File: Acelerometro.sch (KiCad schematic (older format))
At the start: 9 parts, among them Q6 BSS138, Q7 BSS138, U8 MMA7660FC

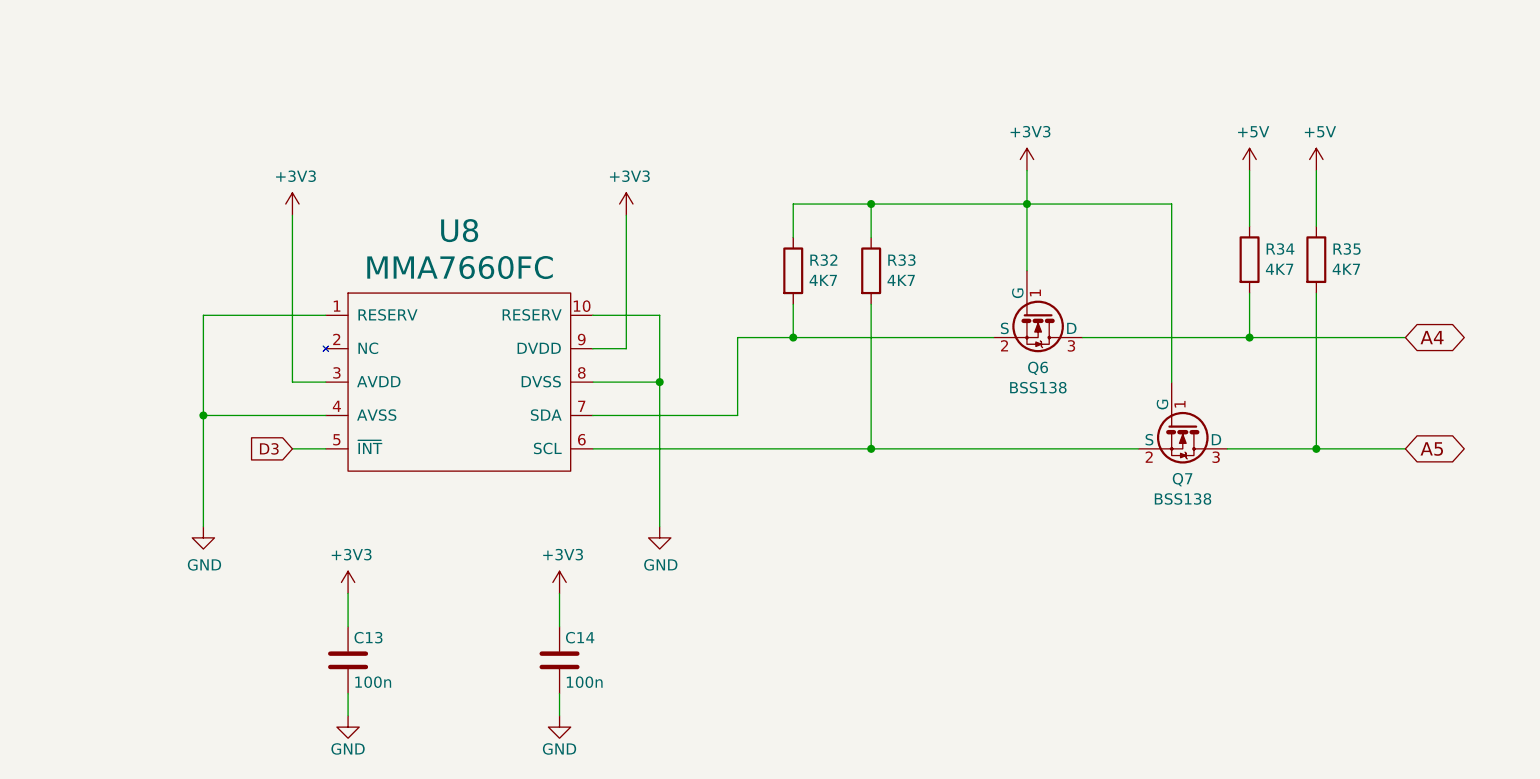
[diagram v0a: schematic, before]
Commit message: Se añade un expansor GPIO al esquema y se elminan registros y codificador
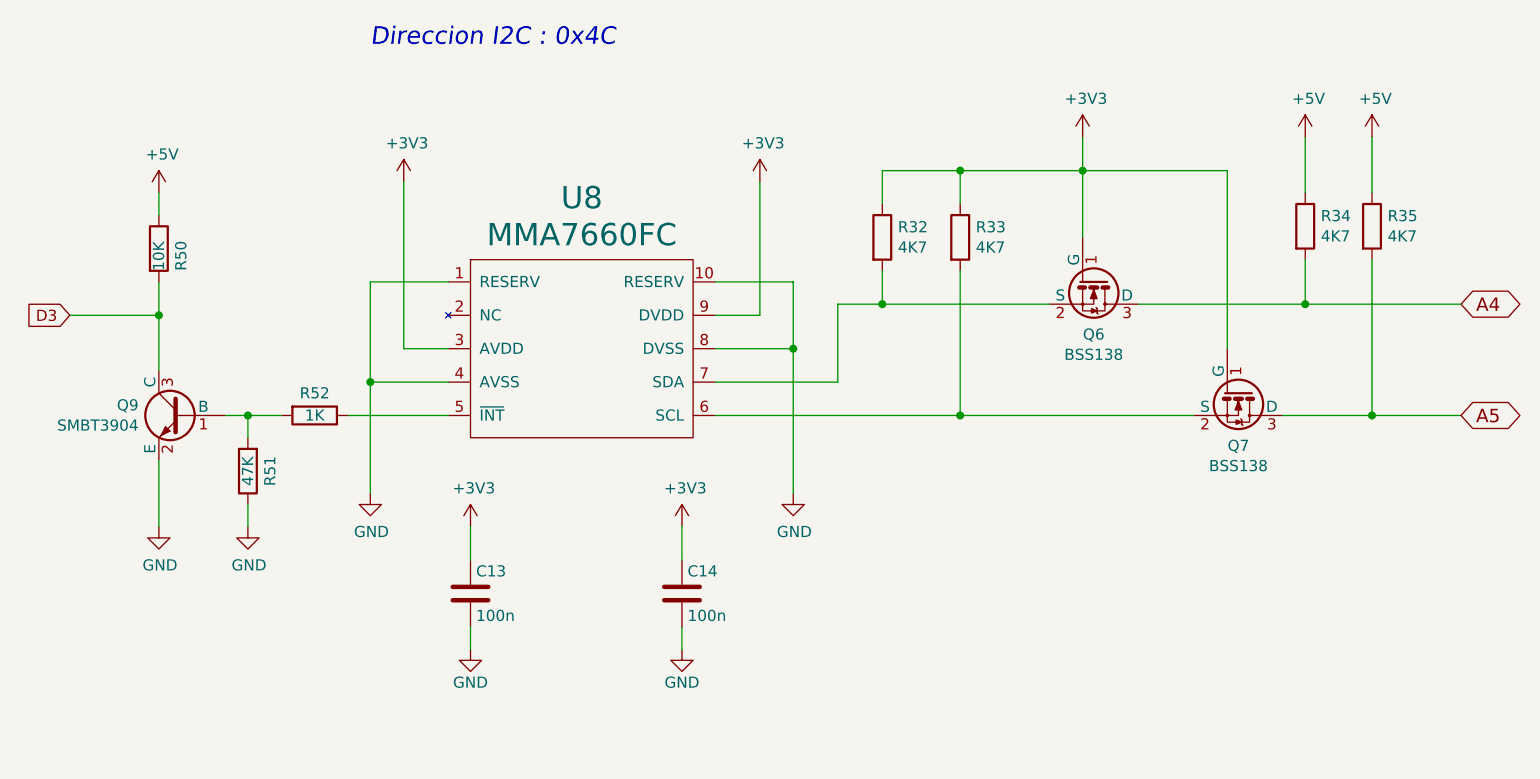
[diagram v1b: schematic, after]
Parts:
- added Q9: SMBT3904, TO_SOT_Packages_SMD:SOT-23, symbol BC849
- added R50: 10K, Resistencias:R_0805, symbol R
- added R51: 47K, Resistencias:R_0805, symbol R
- added R52: 1K, Resistencias:R_0805, symbol R
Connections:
- net +5V: now also R50.1
- net D3: now also Q9.3 (C), R50.2; no longer U8.5 (~INT)
- net GND: now also Q9.2 (E), R51.1
- new net: R52.1, U8.5 (~INT)
- new net: Q9.1 (B), R51.2, R52.2
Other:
- note added: "Direccion I2C : 0x4C"
- moved on the sheet: C13, C14, Q6, Q7, R32, R33, R34, R35, U8

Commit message: finalizada la ubicacion de componentes para la V0.4
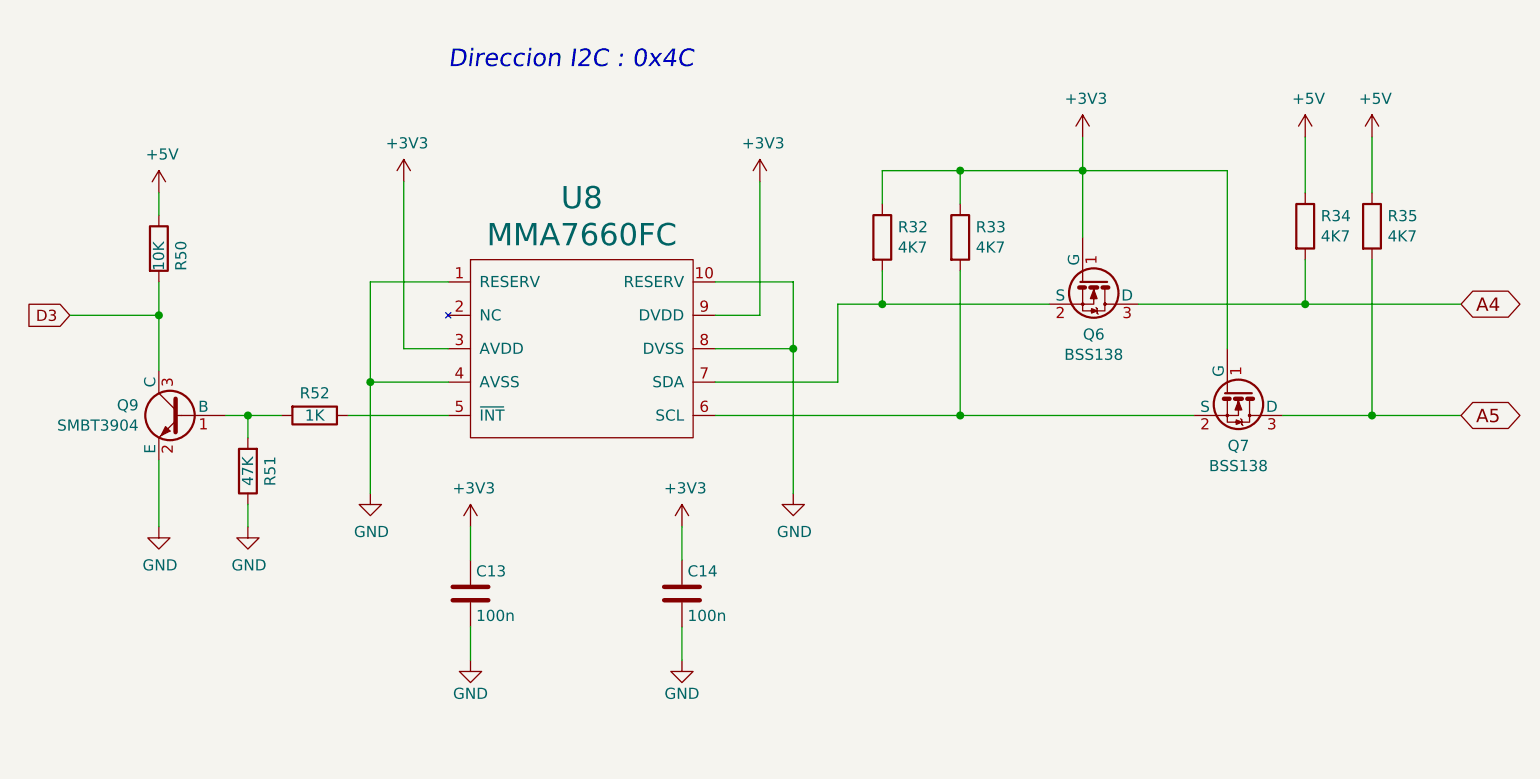
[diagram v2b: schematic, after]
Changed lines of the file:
@@
 	5450 1300 5450 1750
 $Comp
-L +3V3 #PWR064
+L +3V3 #PWR065
 U 1 1 57952AC0
 P 5450 1300
-F 0 "#PWR064" H 5450 1150 50  0001 C CNN
+F 0 "#PWR065" H 5450 1150 50  0001 C CNN
 F 1 "+3V3" H 5465 1473 50  0000 C CNN
 F 2 "" H 5450 1300 50  0000 C CNN
@@
 	6450 1550 6450 1300
 $Comp
-L +5V #PWR065
+L +5V #PWR066
 U 1 1 57952EB0
 P 6450 1300
-F 0 "#PWR065" H 6450 1150 50  0001 C CNN
+F 0 "#PWR066" H 6450 1150 50  0001 C CNN
 F 1 "+5V" H 6465 1473 50  0000 C CNN
 F 2 "" H 6450 1300 50  0000 C CNN
@@
 	6750 1550 6750 1300
 $Comp
-L +5V #PWR066
+L +5V #PWR067
 U 1 1 57952EEB
 P 6750 1300
-F 0 "#PWR066" H 6750 1150 50  0001 C CNN
+F 0 "#PWR067" H 6750 1150 50  0001 C CNN
 F 1 "+5V" H 6765 1473 50  0000 C CNN
 F 2 "" H 6750 1300 50  0000 C CNN
@@
 	4150 1950 4150 2900
 $Comp
-L GND #PWR067
+L GND #PWR068
 U 1 1 579532CA
 P 4150 2900
-F 0 "#PWR067" H 4150 2650 50  0001 C CNN
+F 0 "#PWR068" H 4150 2650 50  0001 C CNN
 F 1 "GND" H 4155 2727 50  0000 C CNN
 F 2 "" H 4150 2900 50  0000 C CNN
@@
 	2250 1950 2250 2900
 $Comp
-L GND #PWR068
+L GND #PWR069
 U 1 1 5795333D
 P 2250 2900
-F 0 "#PWR068" H 2250 2650 50  0001 C CNN
+F 0 "#PWR069" H 2250 2650 50  0001 C CNN
 F 1 "GND" H 2255 2727 50  0000 C CNN
 F 2 "" H 2250 2900 50  0000 C CNN
@@
 	2400 2250 2400 1500
 $Comp
-L +3V3 #PWR069
+L +3V3 #PWR070
 U 1 1 579533C4
 P 2400 1500
-F 0 "#PWR069" H 2400 1350 50  0001 C CNN
+F 0 "#PWR070" H 2400 1350 50  0001 C CNN
 F 1 "+3V3" H 2415 1673 50  0000 C CNN
 F 2 "" H 2400 1500 50  0000 C CNN
@@
 	4000 2100 4000 1500
 $Comp
-L +3V3 #PWR070
+L +3V3 #PWR071
 U 1 1 57953474
 P 4000 1500
-F 0 "#PWR070" H 4000 1350 50  0001 C CNN
+F 0 "#PWR071" H 4000 1350 50  0001 C CNN
 F 1 "+3V3" H 4015 1673 50  0000 C CNN
 F 2 "" H 4000 1500 50  0000 C CNN
@@
 $EndComp
 $Comp
-L GND #PWR071
+L GND #PWR072
 U 1 1 57953EB4
-P 2700 3600
-F 0 "#PWR071" H 2700 3350 50  0001 C CNN
-F 1 "GND" H 2700 3450 50  0000 C CNN
-F 2 "" H 2700 3600 50  0000 C CNN
-F 3 "" H 2700 3600 50  0000 C CNN
-	1    2700 3600
+P 2700 3650
+F 0 "#PWR072" H 2700 3400 50  0001 C CNN
+F 1 "GND" H 2700 3500 50  0000 C CNN
+F 2 "" H 2700 3650 50  0000 C CNN
+F 3 "" H 2700 3650 50  0000 C CNN
+	1    2700 3650
 	1    0    0    -1
 $EndComp
@@
 	2700 3200 2700 3050
 Wire Wire Line
-	2700 3600 2700 3500
+	2700 3650 2700 3500
 $Comp
 L C C14
@@
 $EndComp
 $Comp
-L GND #PWR072
+L GND #PWR073
 U 1 1 57953F7E
-P 3650 3600
-F 0 "#PWR072" H 3650 3350 50  0001 C CNN
-F 1 "GND" H 3650 3450 50  0000 C CNN
-F 2 "" H 3650 3600 50  0000 C CNN
-F 3 "" H 3650 3600 50  0000 C CNN
-	1    3650 3600
+P 3650 3650
+F 0 "#PWR073" H 3650 3400 50  0001 C CNN
+F 1 "GND" H 3650 3500 50  0000 C CNN
+F 2 "" H 3650 3650 50  0000 C CNN
+F 3 "" H 3650 3650 50  0000 C CNN
+	1    3650 3650
 	1    0    0    -1
 $EndComp
@@
 	3650 3200 3650 3050
 Wire Wire Line
-	3650 3600 3650 3500
-$Comp
-L +3V3 #PWR073
+	3650 3650 3650 3500
+$Comp
+L +3V3 #PWR074
 U 1 1 57953FC4
 P 2700 3050
-F 0 "#PWR073" H 2700 2900 50  0001 C CNN
+F 0 "#PWR074" H 2700 2900 50  0001 C CNN
 F 1 "+3V3" H 2715 3223 50  0000 C CNN
 F 2 "" H 2700 3050 50  0000 C CNN
@@
 $EndComp
 $Comp
-L +3V3 #PWR074
+L +3V3 #PWR075
 U 1 1 57954005
 P 3650 3050
-F 0 "#PWR074" H 3650 2900 50  0001 C CNN
+F 0 "#PWR075" H 3650 2900 50  0001 C CNN
 F 1 "+3V3" H 3665 3223 50  0000 C CNN
 F 2 "" H 3650 3050 50  0000 C CNN
@@
 Text GLabel 900  2100 0    50   Input ~ 0
 D3
-Text Notes 2250 900  0    79   Italic 0
+Text Notes 2600 1000 0    79   Italic 0
 Direccion I2C : 0x4C
 $Comp
@@
 	1300 2750 1300 3050
 $Comp
-L GND #PWR075
+L GND #PWR076
 U 1 1 5881543D
 P 1300 3050
-F 0 "#PWR075" H 1300 2800 50  0001 C CNN
+F 0 "#PWR076" H 1300 2800 50  0001 C CNN
 F 1 "GND" H 1305 2877 50  0000 C CNN
 F 2 "" H 1300 3050 50  0000 C CNN
@@
 Connection ~ 1700 2550
 $Comp
-L GND #PWR076
+L GND #PWR077
 U 1 1 58815452
 P 1700 3050
-F 0 "#PWR076" H 1700 2800 50  0001 C CNN
+F 0 "#PWR077" H 1700 2800 50  0001 C CNN
 F 1 "GND" H 1705 2877 50  0000 C CNN
 F 2 "" H 1700 3050 50  0000 C CNN
@@
 	1300 1650 1300 1550
 $Comp
-L +5V #PWR077
+L +5V #PWR078
 U 1 1 58815BF6
 P 1300 1550
-F 0 "#PWR077" H 1300 1400 50  0001 C CNN
+F 0 "#PWR078" H 1300 1400 50  0001 C CNN
 F 1 "+5V" H 1315 1723 50  0000 C CNN
 F 2 "" H 1300 1550 50  0000 C CNN

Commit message: Revisado V0.4. Actualizados gerber y esquemas
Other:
- note added: "Configurar ~INT\nactiva a nivel alto y push-pull"
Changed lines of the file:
@@
 Sheet 13 17
 Title "Acelerometro 3 ejes"
-Date "2017-01-19"
+Date "2017-01-25"
 Rev "V.0.4"
 Comp "NanoPlayBoard"
@@
 $EndComp
 Wire Wire Line
+	1300 1950 1300 2350
+Wire Wire Line
+	2600 2550 2150 2550
+Wire Wire Line
+	1300 2100 900  2100
+$Comp
+L R R50
+U 1 1 58815BED
+P 1300 1800
+F 0 "R50" V 1400 1700 50  0000 L CNN
+F 1 "10K" V 1300 1700 50  0000 L CNN
+F 2 "Resistencias:R_0805" V 1230 1800 50  0001 C CNN
+F 3 "" H 1300 1800 50  0000 C CNN
+F 4 "VISHAY" H 1300 1800 60  0001 C CNN "Fabricante"
+F 5 "CRCW080510K0FKEA" H 1300 1800 60  0001 C CNN "Ref"
+F 6 "1/8W" H 1300 1800 60  0001 C CNN "Potencia"
+F 7 "1%" H 1300 1800 60  0001 C CNN "Tolerancia"
+F 8 "TME" H 1300 1800 60  0001 C CNN "Provedor"
+F 9 "CRCW080510K0FKEA" H 1300 1800 60  0001 C CNN "Ref_Proveedor"
+	1    1300 1800
+	1    0    0    -1
+$EndComp
+Wire Wire Line
+	1300 1650 1300 1550
+$Comp
+L +5V #PWR078
+U 1 1 58815BF6
+P 1300 1550
+F 0 "#PWR078" H 1300 1400 50  0001 C CNN
+F 1 "+5V" H 1315 1723 50  0000 C CNN
+F 2 "" H 1300 1550 50  0000 C CNN
+F 3 "" H 1300 1550 50  0000 C CNN
+	1    1300 1550
+	1    0    0    -1
+$EndComp
+Connection ~ 1300 2100
+Wire Wire Line
 	1600 2550 1850 2550
-Wire Wire Line
-	1300 1950 1300 2350
 Wire Wire Line
 	1300 2750 1300 3050
@@
 	1    0    0    -1
 $EndComp
+$Comp
+L GND #PWR077
+U 1 1 58815452
+P 1700 3050
+F 0 "#PWR077" H 1700 2800 50  0001 C CNN
+F 1 "GND" H 1705 2877 50  0000 C CNN
+F 2 "" H 1700 3050 50  0000 C CNN
+F 3 "" H 1700 3050 50  0000 C CNN
+	1    1700 3050
+	1    0    0    -1
+$EndComp
+Connection ~ 1700 2550
+Wire Wire Line
+	1700 2650 1700 2550
+Wire Wire Line
+	1700 3050 1700 2950
 $Comp
 L R R51
@@
 	-1   0    0    1
 $EndComp
-Wire Wire Line
-	1700 2650 1700 2550
-Connection ~ 1700 2550
-$Comp
-L GND #PWR077
-U 1 1 58815452
-P 1700 3050
-F 0 "#PWR077" H 1700 2800 50  0001 C CNN
-F 1 "GND" H 1705 2877 50  0000 C CNN
-F 2 "" H 1700 3050 50  0000 C CNN
-F 3 "" H 1700 3050 50  0000 C CNN
-	1    1700 3050
-	1    0    0    -1
-$EndComp
-Wire Wire Line
-	1700 3050 1700 2950
-Wire Wire Line
-	2600 2550 2150 2550
-Wire Wire Line
-	1300 2100 900  2100
-$Comp
-L R R50
-U 1 1 58815BED
-P 1300 1800
-F 0 "R50" V 1400 1700 50  0000 L CNN
-F 1 "10K" V 1300 1700 50  0000 L CNN
-F 2 "Resistencias:R_0805" V 1230 1800 50  0001 C CNN
-F 3 "" H 1300 1800 50  0000 C CNN
-F 4 "VISHAY" H 1300 1800 60  0001 C CNN "Fabricante"
-F 5 "CRCW080510K0FKEA" H 1300 1800 60  0001 C CNN "Ref"
-F 6 "1/8W" H 1300 1800 60  0001 C CNN "Potencia"
-F 7 "1%" H 1300 1800 60  0001 C CNN "Tolerancia"
-F 8 "TME" H 1300 1800 60  0001 C CNN "Provedor"
-F 9 "CRCW080510K0FKEA" H 1300 1800 60  0001 C CNN "Ref_Proveedor"
-	1    1300 1800
-	1    0    0    -1
-$EndComp
-Wire Wire Line
-	1300 1650 1300 1550
-$Comp
-L +5V #PWR078
-U 1 1 58815BF6
-P 1300 1550
-F 0 "#PWR078" H 1300 1400 50  0001 C CNN
-F 1 "+5V" H 1315 1723 50  0000 C CNN
-F 2 "" H 1300 1550 50  0000 C CNN
-F 3 "" H 1300 1550 50  0000 C CNN
-	1    1300 1550
-	1    0    0    -1
-$EndComp
-Connection ~ 1300 2100
+Text Notes 1200 3600 0    47   ~ 0
+Configurar ~INT\nactiva a nivel alto y push-pull
 $EndSCHEMATC

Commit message: finalizada V0.4.1 corrige #17, #18 y #19
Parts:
- Q6, Q7: symbol BSS138 -> BSS138-RESCUE-Nano_PB
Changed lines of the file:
@@
 LIBS:Pasivos
 LIBS:Reles
+LIBS:Arduino
 LIBS:Nano_PB-cache
 EELAYER 26 0
@@
 $EndDescr
 $Comp
-L BSS138 Q6
+L BSS138-RESCUE-Nano_PB Q6
 U 1 1 57952913
 P 5500 1950
@@
 	5450 1300 5450 1750
 $Comp
-L +3V3 #PWR057
+L +3V3 #PWR058
 U 1 1 57952AC0
 P 5450 1300
-F 0 "#PWR057" H 5450 1150 50  0001 C CNN
+F 0 "#PWR058" H 5450 1150 50  0001 C CNN
 F 1 "+3V3" H 5465 1473 50  0000 C CNN
 F 2 "" H 5450 1300 50  0000 C CNN
@@
 A5
 $Comp
-L BSS138 Q7
+L BSS138-RESCUE-Nano_PB Q7
 U 1 1 57952D65
 P 6150 2450
@@
 	6450 1550 6450 1300
 $Comp
-L +5V #PWR058
+L +5V #PWR059
 U 1 1 57952EB0
 P 6450 1300
-F 0 "#PWR058" H 6450 1150 50  0001 C CNN
+F 0 "#PWR059" H 6450 1150 50  0001 C CNN
 F 1 "+5V" H 6465 1473 50  0000 C CNN
 F 2 "" H 6450 1300 50  0000 C CNN
@@
 	6750 1550 6750 1300
 $Comp
-L +5V #PWR059
+L +5V #PWR060
 U 1 1 57952EEB
 P 6750 1300
-F 0 "#PWR059" H 6750 1150 50  0001 C CNN
+F 0 "#PWR060" H 6750 1150 50  0001 C CNN
 F 1 "+5V" H 6765 1473 50  0000 C CNN
 F 2 "" H 6750 1300 50  0000 C CNN
@@
 	4150 1950 4150 2900
 $Comp
-L GND #PWR060
+L GND #PWR061
 U 1 1 579532CA
 P 4150 2900
-F 0 "#PWR060" H 4150 2650 50  0001 C CNN
+F 0 "#PWR061" H 4150 2650 50  0001 C CNN
 F 1 "GND" H 4155 2727 50  0000 C CNN
 F 2 "" H 4150 2900 50  0000 C CNN
@@
 	2250 1950 2250 2900
 $Comp
-L GND #PWR061
+L GND #PWR062
 U 1 1 5795333D
 P 2250 2900
-F 0 "#PWR061" H 2250 2650 50  0001 C CNN
+F 0 "#PWR062" H 2250 2650 50  0001 C CNN
 F 1 "GND" H 2255 2727 50  0000 C CNN
 F 2 "" H 2250 2900 50  0000 C CNN
@@
 	2400 2250 2400 1500
 $Comp
-L +3V3 #PWR062
+L +3V3 #PWR063
 U 1 1 579533C4
 P 2400 1500
-F 0 "#PWR062" H 2400 1350 50  0001 C CNN
+F 0 "#PWR063" H 2400 1350 50  0001 C CNN
 F 1 "+3V3" H 2415 1673 50  0000 C CNN
 F 2 "" H 2400 1500 50  0000 C CNN
@@
 	4000 2100 4000 1500
 $Comp
-L +3V3 #PWR063
+L +3V3 #PWR064
 U 1 1 57953474
 P 4000 1500
-F 0 "#PWR063" H 4000 1350 50  0001 C CNN
+F 0 "#PWR064" H 4000 1350 50  0001 C CNN
 F 1 "+3V3" H 4015 1673 50  0000 C CNN
 F 2 "" H 4000 1500 50  0000 C CNN
@@
 $EndComp
 $Comp
-L GND #PWR064
+L GND #PWR065
 U 1 1 57953EB4
 P 2700 3650
-F 0 "#PWR064" H 2700 3400 50  0001 C CNN
+F 0 "#PWR065" H 2700 3400 50  0001 C CNN
 F 1 "GND" H 2700 3500 50  0000 C CNN
 F 2 "" H 2700 3650 50  0000 C CNN
@@
 $EndComp
 $Comp
-L GND #PWR065
+L GND #PWR066
 U 1 1 57953F7E
 P 3650 3650
-F 0 "#PWR065" H 3650 3400 50  0001 C CNN
+F 0 "#PWR066" H 3650 3400 50  0001 C CNN
 F 1 "GND" H 3650 3500 50  0000 C CNN
 F 2 "" H 3650 3650 50  0000 C CNN
@@
 	3650 3650 3650 3500
 $Comp
-L +3V3 #PWR066
+L +3V3 #PWR067
 U 1 1 57953FC4
 P 2700 3050
-F 0 "#PWR066" H 2700 2900 50  0001 C CNN
+F 0 "#PWR067" H 2700 2900 50  0001 C CNN
 F 1 "+3V3" H 2715 3223 50  0000 C CNN
 F 2 "" H 2700 3050 50  0000 C CNN
@@
 $EndComp
 $Comp
-L +3V3 #PWR067
+L +3V3 #PWR068
 U 1 1 57954005
 P 3650 3050
-F 0 "#PWR067" H 3650 2900 50  0001 C CNN
+F 0 "#PWR068" H 3650 2900 50  0001 C CNN
 F 1 "+3V3" H 3665 3223 50  0000 C CNN
 F 2 "" H 3650 3050 50  0000 C CNN
@@
 	1300 1650 1300 1550
 $Comp
-L +5V #PWR068
+L +5V #PWR069
 U 1 1 58815BF6
 P 1300 1550
-F 0 "#PWR068" H 1300 1400 50  0001 C CNN
+F 0 "#PWR069" H 1300 1400 50  0001 C CNN
 F 1 "+5V" H 1315 1723 50  0000 C CNN
 F 2 "" H 1300 1550 50  0000 C CNN
@@
 	1300 2750 1300 3050
 $Comp
-L GND #PWR069
+L GND #PWR070
 U 1 1 5881543D
 P 1300 3050
-F 0 "#PWR069" H 1300 2800 50  0001 C CNN
+F 0 "#PWR070" H 1300 2800 50  0001 C CNN
 F 1 "GND" H 1305 2877 50  0000 C CNN
 F 2 "" H 1300 3050 50  0000 C CNN
@@
 $EndComp
 $Comp
-L GND #PWR070
+L GND #PWR071
 U 1 1 58815452
 P 1700 3050
-F 0 "#PWR070" H 1700 2800 50  0001 C CNN
+F 0 "#PWR071" H 1700 2800 50  0001 C CNN
 F 1 "GND" H 1705 2877 50  0000 C CNN
 F 2 "" H 1700 3050 50  0000 C CNN
